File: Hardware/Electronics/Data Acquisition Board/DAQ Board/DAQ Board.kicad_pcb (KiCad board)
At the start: 4 copper layers, 107.2 x 58.8 mm, 131 parts, among them J1 Conn_01x09_Male, J2 USB_B_Mini, J3 Battery Connector, J4 DC Barrel Jack, J5 HC-05 BT Module, J6 ICSP Header, Q1 DMP2100U, SW1 DIP, SW10 SW_SPDT, SW11 SW_SPDT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

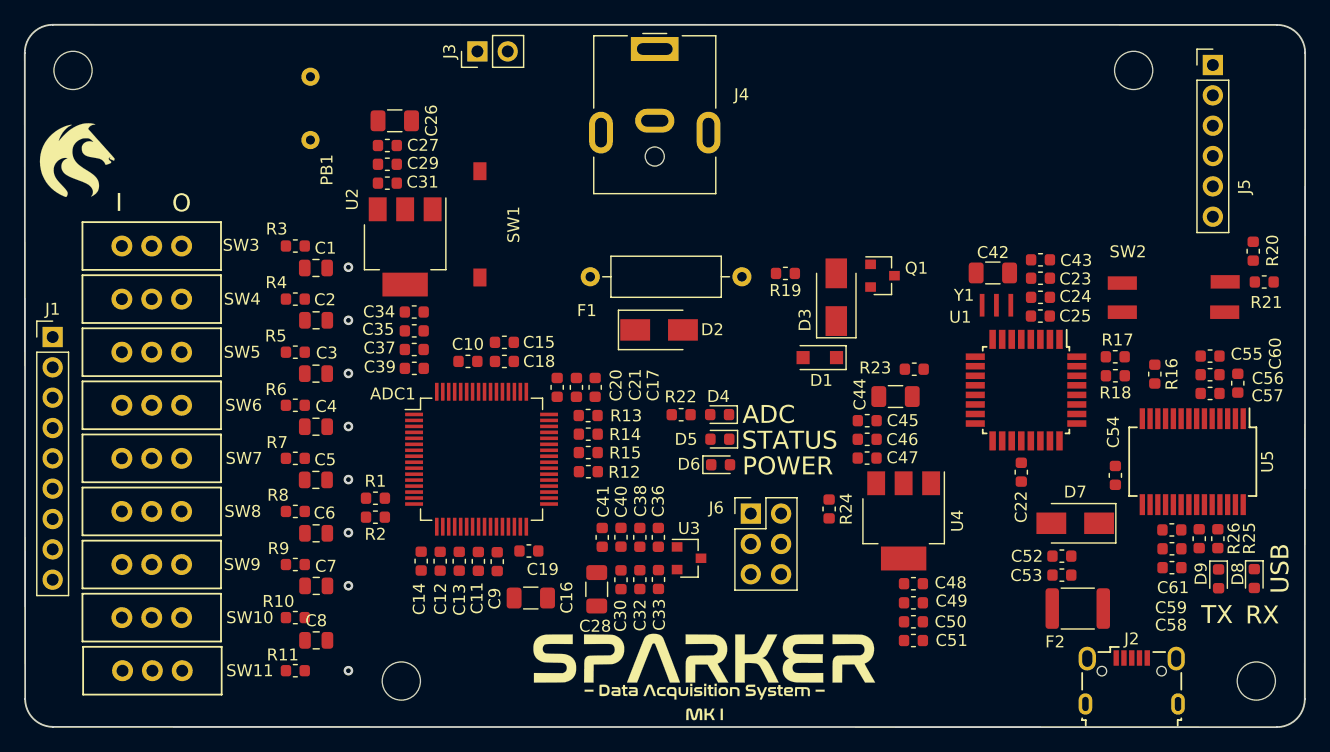
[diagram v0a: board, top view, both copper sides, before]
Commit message: Started layout, added MCU datasheet
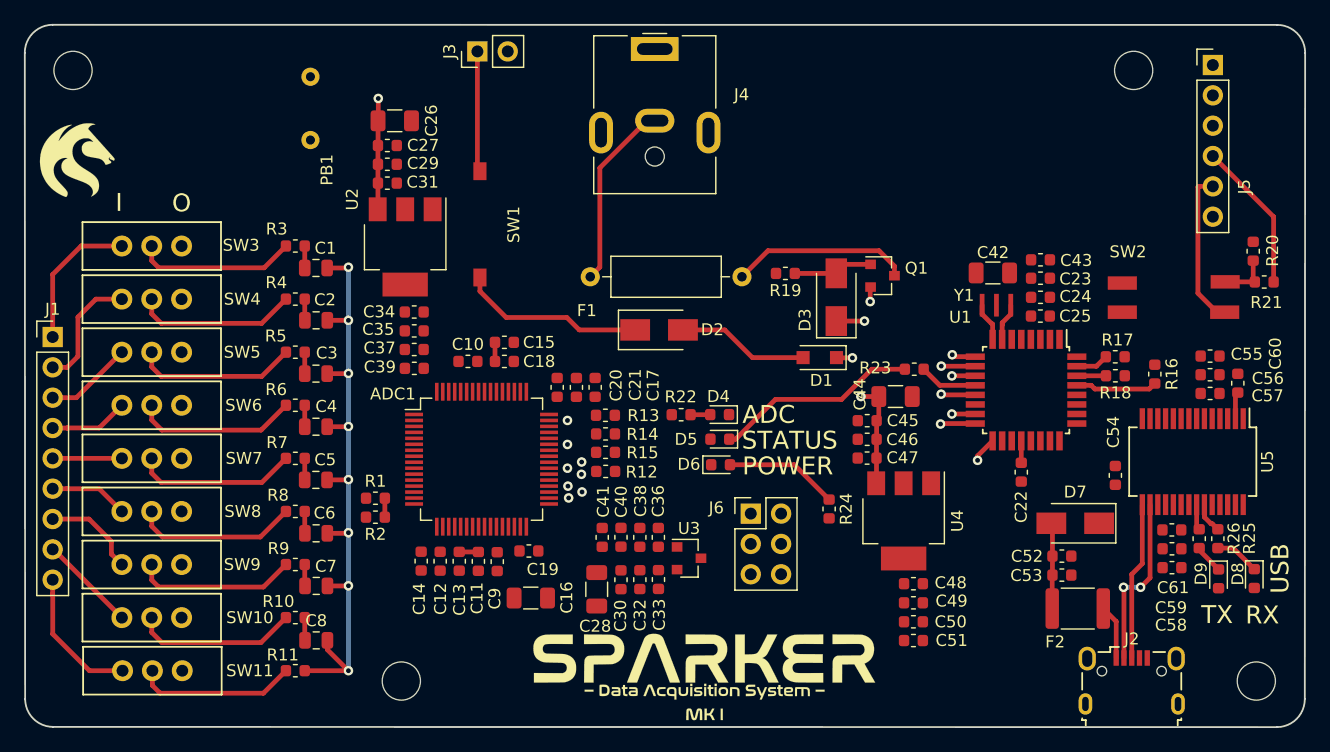
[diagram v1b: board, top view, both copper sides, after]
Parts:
- moved R13 1.45 mm to (68.4, 98.2)
- moved R14 1.45 mm to (68.5, 99.7)
- moved R15 1.45 mm to (68.5, 101.3)
- moved R12 1.45 mm to (68.5, 102.9)
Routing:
- net Net-(ADC1-Pad17): track 0.00 -> 53.2 mm
- net /VIN: track 0.00 -> 23.1 mm, vias 0 -> 5
- net Net-(D5-Pad1): track 0.00 -> 17.1 mm
- net /VIN_RAW: track 0.00 -> 15.7 mm
- net Net-(D2-Pad1): track 0.00 -> 15.5 mm
- net Net-(F1-Pad1): track 0.00 -> 15.0 mm
- net Net-(J2-Pad2): track 0.00 -> 14.6 mm, vias 0 -> 2
- net Net-(R8-Pad2): track 0.00 -> 13.7 mm
- net Net-(R10-Pad2): track 0.00 -> 13.7 mm
- net Net-(R6-Pad2): track 0.00 -> 13.7 mm
- net Net-(R4-Pad2): track 0.00 -> 13.6 mm
- net Net-(R5-Pad2): track 0.00 -> 13.6 mm
- net Net-(R7-Pad2): track 0.00 -> 13.6 mm
- net Net-(R9-Pad2): track 0.00 -> 13.6 mm
- net Net-(R3-Pad2): track 0.00 -> 13.5 mm
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- added copper zone on In1.Cu, net /+5V
- added copper zone on In1.Cu, net /ADC1299/AVDD
- added copper zone on In1.Cu, net /VIN
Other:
- net class Default: trace_width 0.25 -> 0.4

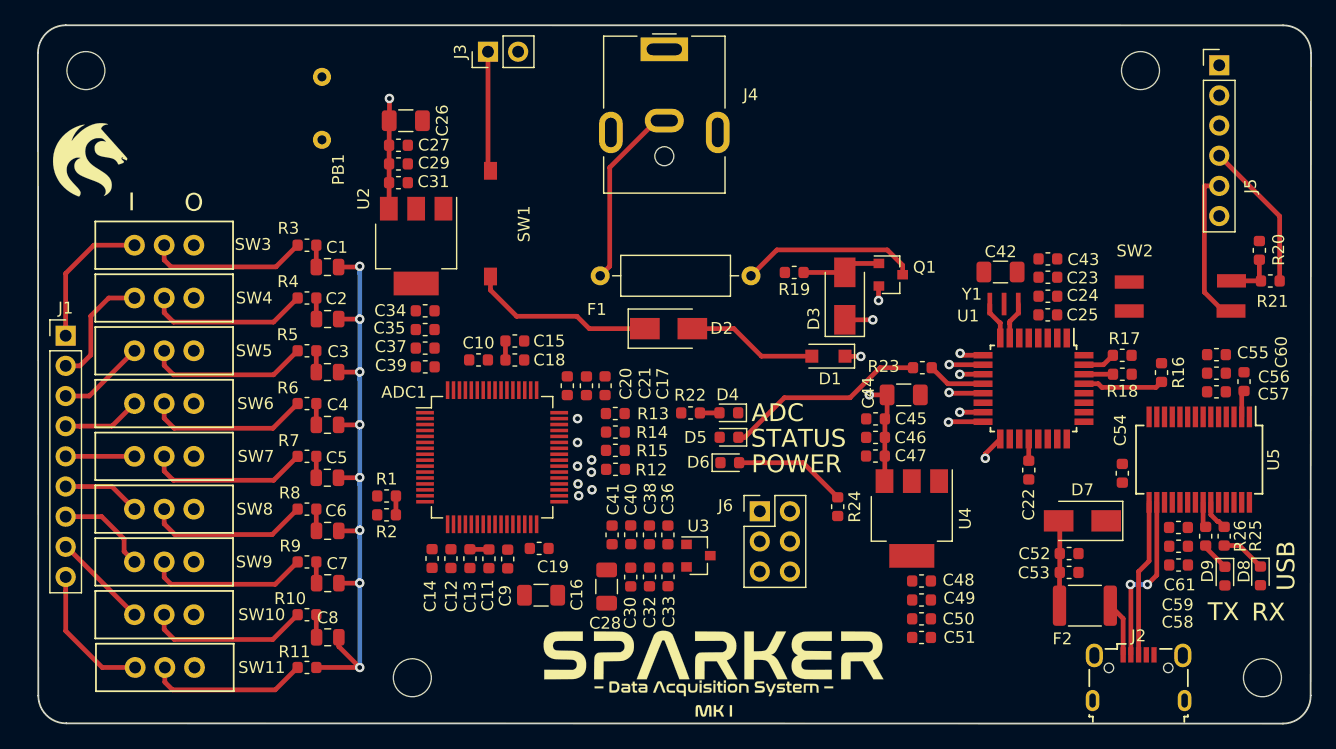
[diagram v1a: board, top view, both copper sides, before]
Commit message: Shrank the board, changed out PB, changed 9 pin header for a a shrouded one
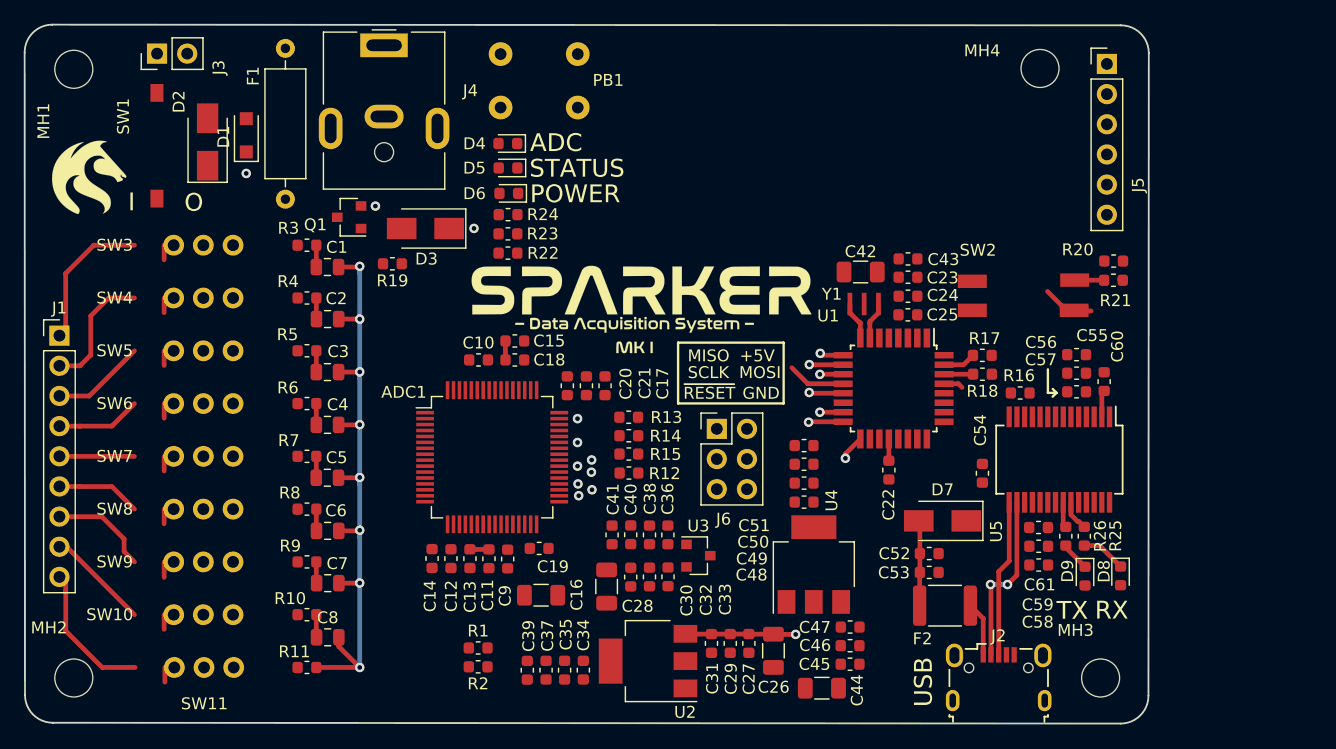
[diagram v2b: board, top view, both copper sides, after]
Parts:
- removed ?: , Sparker:UoN
- removed ? (x4): MountingHole, MountingHole:MountingHole_3.2mm_M3
- removed G***: LOGO, Sparker:NASA
- removed G***: LOGO, Sparker:NASA_subtext
- added LOGO1: UoNLogo, Sparker:UoN, F.Cu at (24.1, 78.3)
- added LOGO2: SparkerLogo, Sparker:NASA, F.Cu at (70.6, 87.9)
- added MH1: MountingHole, MountingHole:MountingHole_3.2mm_M3, F.Cu at (22.8, 69.2)
- added MH2: MountingHole, MountingHole:MountingHole_3.2mm_M3, F.Cu at (22.8, 120.4)
- added MH3: MountingHole, MountingHole:MountingHole_3.2mm_M3, F.Cu at (109.3, 120.4)
- added MH4: MountingHole, MountingHole:MountingHole_3.2mm_M3, F.Cu at (104.2, 69.1)
- added TEXT1: Text, Sparker:NASA_subtext, F.Cu at (70.0, 91.6)
- J1: footprint Connector_PinHeader_2.54mm:PinHeader_1x09_P2.54mm_Vertical -> Connectors:TE-5-103669-8
- PB1: value RESET -> TE-1825910-6; footprint GPTS203211B:GPTS203211B -> Switches:1825910-6
- moved C26 54.3 mm to (81.8, 118.2), turned to 270 degrees
- moved D1 52.4 mm to (37.4, 74.7), turned to 90 degrees
- moved C27 51.3 mm to (79.7, 117.5), turned to 270 degrees
- moved C29 49.1 mm to (78.1, 117.5), turned to 270 degrees
- moved C31 46.9 mm to (76.5, 117.5), turned to 270 degrees
- moved Q1 45.9 mm to (46.0, 81.6), turned to 180 degrees
- moved D2 41.9 mm to (34.1, 75.3), turned to 90 degrees
- moved U2 40.0 mm to (71.2, 119.0), turned to 180 degrees
- moved F1 39.7 mm to (40.7, 80.1), turned to 90 degrees
- moved R24 37.1 mm to (59.4, 81.4), turned to 0 degrees
- moved R23 36.7 mm to (59.4, 83.0)
- moved D3 35.8 mm to (52.5, 82.6), turned to 180 degrees
- moved R19 33.8 mm to (49.7, 85.6)
- moved C34 33.1 mm to (65.8, 119.8), turned to 270 degrees
- moved C35 31.0 mm to (64.2, 119.8), turned to 270 degrees
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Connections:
- D5 pad 1: Net-(D5-Pad1) -> /GND
- D5 pad 2: /+5V -> Net-(D5-Pad2)
- PB1 pad 2: /GND -> /ADC1299/~RESET
- R23 pad 1: Net-(D5-Pad1) -> Net-(D5-Pad2)
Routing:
- net Net-(D5-Pad1): track 17.1 -> 0.00 mm
- net /VIN_RAW: track 15.7 -> 0.00 mm
- net Net-(D2-Pad1): track 15.5 -> 0.00 mm
- net Net-(F1-Pad1): track 15.0 -> 0.00 mm
- net /VIN: track 23.1 -> 9.30 mm, vias 5 -> 4
- net Net-(R8-Pad2): track 13.7 -> 0.00 mm
- net Net-(R10-Pad2): track 13.7 -> 0.00 mm
- net Net-(R6-Pad2): track 13.7 -> 0.00 mm
- net Net-(R4-Pad2): track 13.6 -> 0.00 mm
- net Net-(R5-Pad2): track 13.6 -> 0.00 mm
- net Net-(R7-Pad2): track 13.6 -> 0.00 mm
- net Net-(R9-Pad2): track 13.6 -> 0.00 mm
- net Net-(R3-Pad2): track 13.5 -> 0.00 mm
- net Net-(R11-Pad2): track 13.5 -> 0.00 mm
- net /HC05_RX: track 12.7 -> 0.20 mm
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- removed copper zone on In1.Cu, net /+5V
- removed copper zone on In1.Cu, net /ADC1299/AVDD
- removed copper zone on In1.Cu, net /VIN
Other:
- board size 107.2 x 58.8 mm -> 94.7 x 58.9 mm
- board text added: "+5V"
- board text added: "GND"
- board text added: "MISO"
- board text added: "MOSI"
- board text added: "SCLK"
- board text added: "~RESET"

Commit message: Small changes
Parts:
- moved C2 1.85 mm to (44.2, 92.1)
- moved C6 1.85 mm to (44.2, 109.9)
- moved C7 1.85 mm to (44.2, 114.3)
- moved R4 1.85 mm to (42.5, 90.3)
- moved R6 1.85 mm to (42.5, 99.2)
- moved C1 1.85 mm to (44.2, 87.7)
- moved C3 1.85 mm to (44.2, 96.5)
- moved C4 1.85 mm to (44.2, 101.0)
- moved C5 1.85 mm to (44.2, 105.4)
- moved C8 1.85 mm to (44.2, 118.9)
- moved R10 1.85 mm to (42.5, 117.0)
- moved R11 1.85 mm to (42.5, 121.4)
- moved R3 1.85 mm to (42.5, 85.8)
- moved R5 1.85 mm to (42.5, 94.7)
- moved R7 1.85 mm to (42.5, 103.6)
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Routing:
- net Net-(J1-Pad1): track 13.3 -> 0.00 mm
- net Net-(J1-Pad9): track 12.9 -> 0.00 mm
- net Net-(J1-Pad2): track 11.3 -> 0.00 mm
- net Net-(J1-Pad8): track 9.40 -> 0.08 mm
- net Net-(J1-Pad7): track 9.30 -> 0.00 mm
- net Net-(J1-Pad3): track 8.61 -> 0.00 mm
- net Net-(J1-Pad6): track 7.82 -> 0.00 mm
- net Net-(J1-Pad4): track 7.82 -> 0.00 mm
- net Net-(J1-Pad5): track 7.03 -> 0.00 mm
- net /VIN: track 9.30 -> 14.4 mm
